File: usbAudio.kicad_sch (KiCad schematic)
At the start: 4 parts, among them J1 12V in, J2 USB_C_Receptacle_USB2.0_14P, J3 AudioJack3, U1 PCM2705CDBR

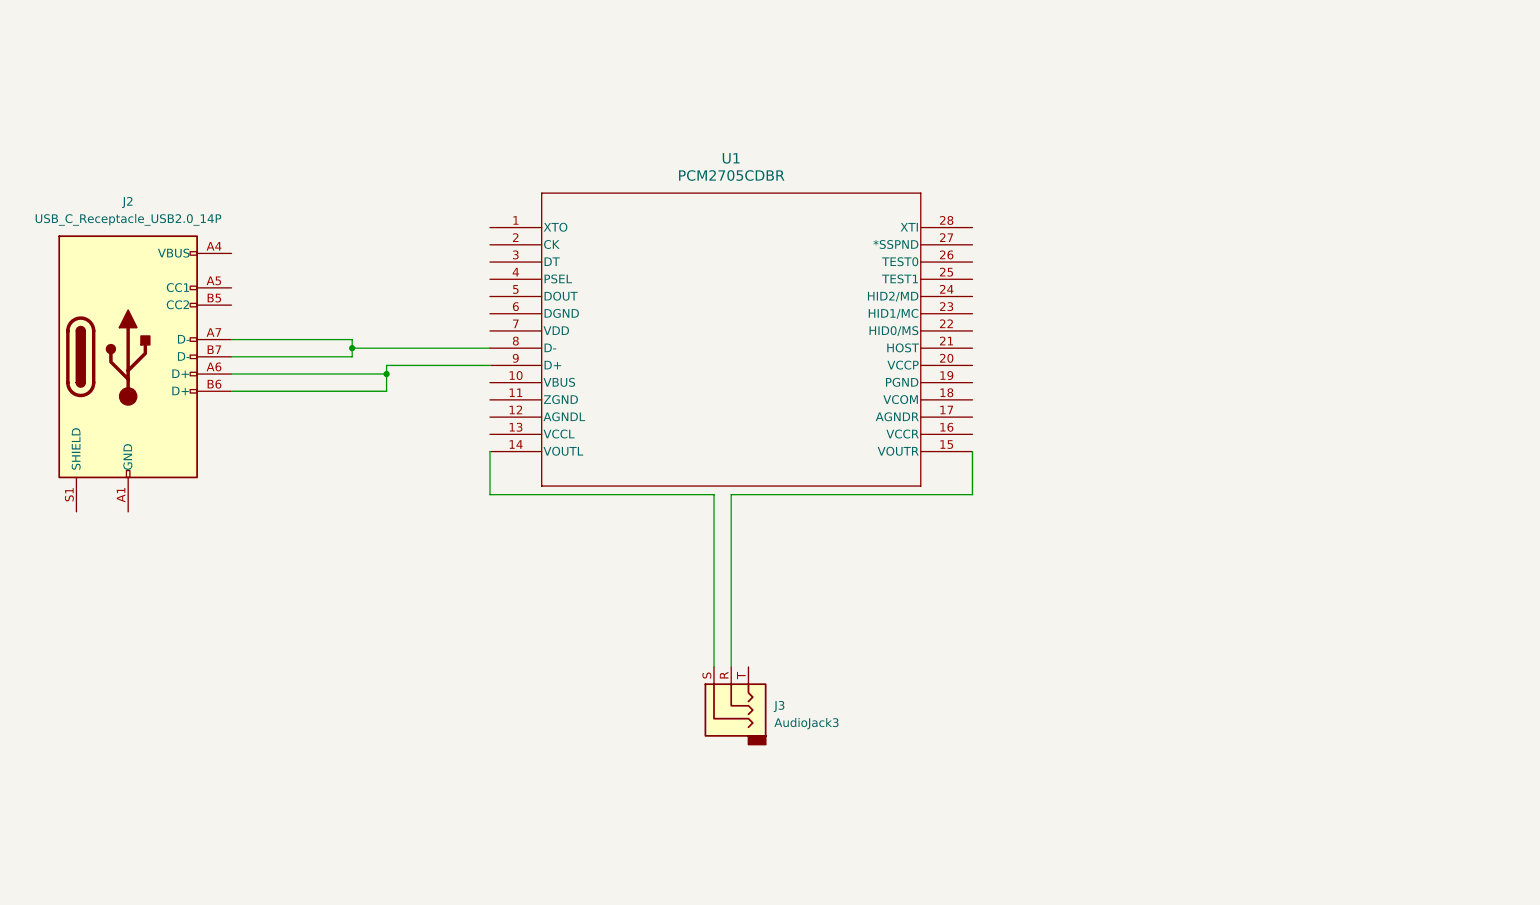
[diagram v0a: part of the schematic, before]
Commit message: Work on setting up audio IC
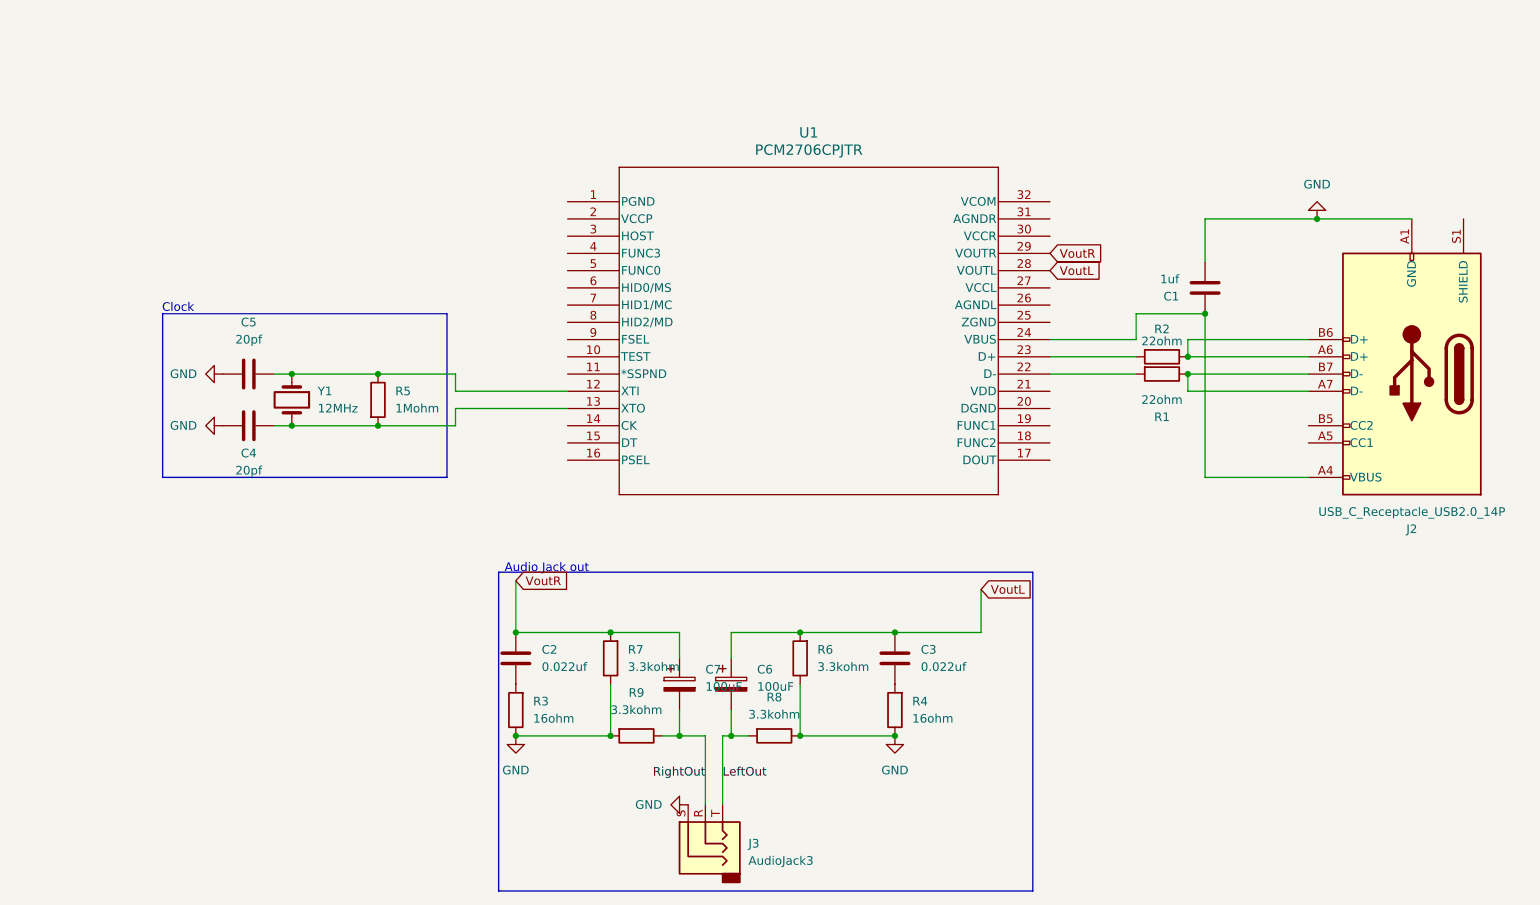
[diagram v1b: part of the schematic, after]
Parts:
- removed U1: PCM2705CDBR, DB28, symbol PCM2705C:PCM2705CDBR
- added C1: 1uf, symbol Device:C
- added C2, C3: 0.022uf, symbol Device:C
- added C4, C5: 20pf, symbol Device:C
- added C6, C7: 100uF, symbol Device:C_Polarized
- added R1, R2: 22ohm, symbol Device:R
- added R3, R4: 16ohm, symbol Device:R
- added R5: 1Mohm, symbol Device:R
- added R6, R7, R8, R9: 3.3kohm, symbol Device:R
- added U1: PCM2706CPJTR, PJT32, symbol PCM2706C:PCM2706CPJTR
- added Y1: 12MHz, symbol Device:Crystal
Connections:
- net RightOut: now reaches J3.R
- net RightOut: now also C7.2, R9.1
- net GND: now reaches J3.S
- net GND: now also J2.A1 (GND), J2.A12 (GND), J2.B1 (GND), J2.B12 (GND), C1.1, C4.2, C5.2, R3.1, R4.1, R6.1, R7.1, R8.1, R9.2
- net LeftOut: now reaches J3.T
- net LeftOut: now also C6.2, R8.2
- net at J2.A4 (VBUS), J2.A9 (VBUS), J2.B4 (VBUS)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: now also C1.2, U1.24 (VBUS)
- net at J2.A6 (D+), J2.B6 (D+): now also R2.1
- net at J2.A7 (D-), J2.B7 (D-): now also R1.1
- new net: C5.1, R5.1, U1.12 (XTI), Y1.1
- new net: C4.1, R5.2, U1.13 (XTO), Y1.2
- new net: R1.2, U1.22 (D-)
- new net: R2.2, U1.23 (D+)
- new net: C2.1, R3.2
- new net: C3.1, R4.2
- new net VoutL: C3.2, C6.1, R6.2, U1.28 (VOUTL)
- new net VoutR: C2.2, C7.1, R7.2, U1.29 (VOUTR)
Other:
- note added: "Audio Jack out"
- note added: "Clock"
- moved on the sheet: J2, J3

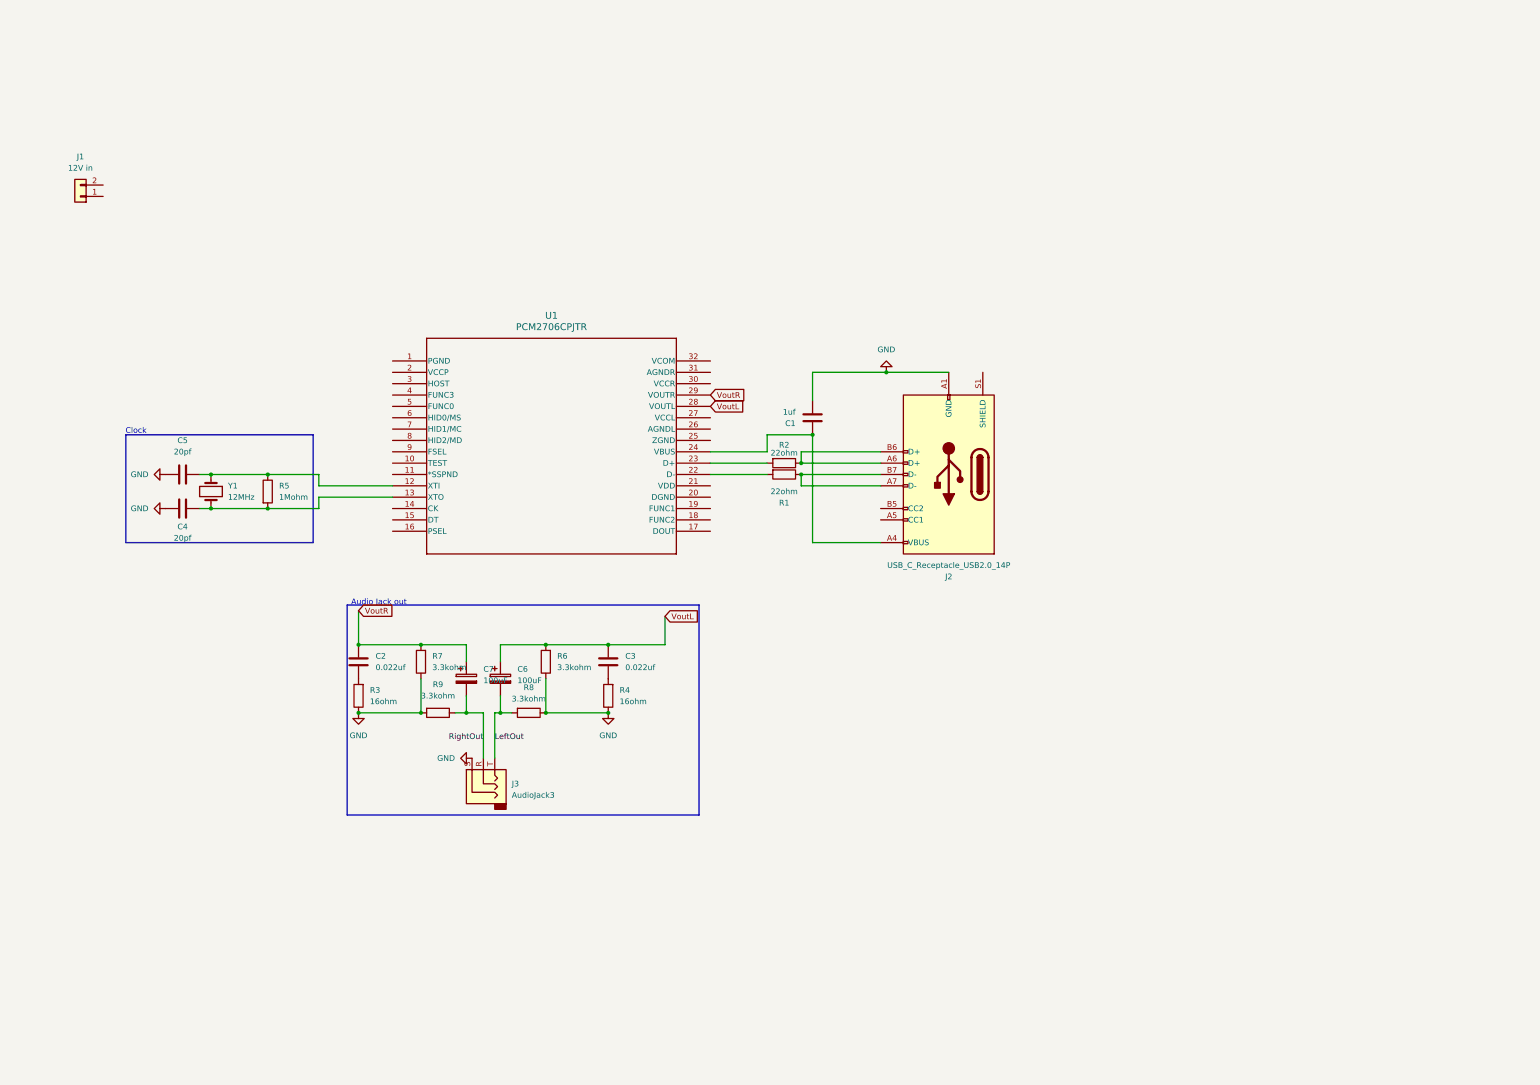
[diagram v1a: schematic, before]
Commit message: Finish audio IC
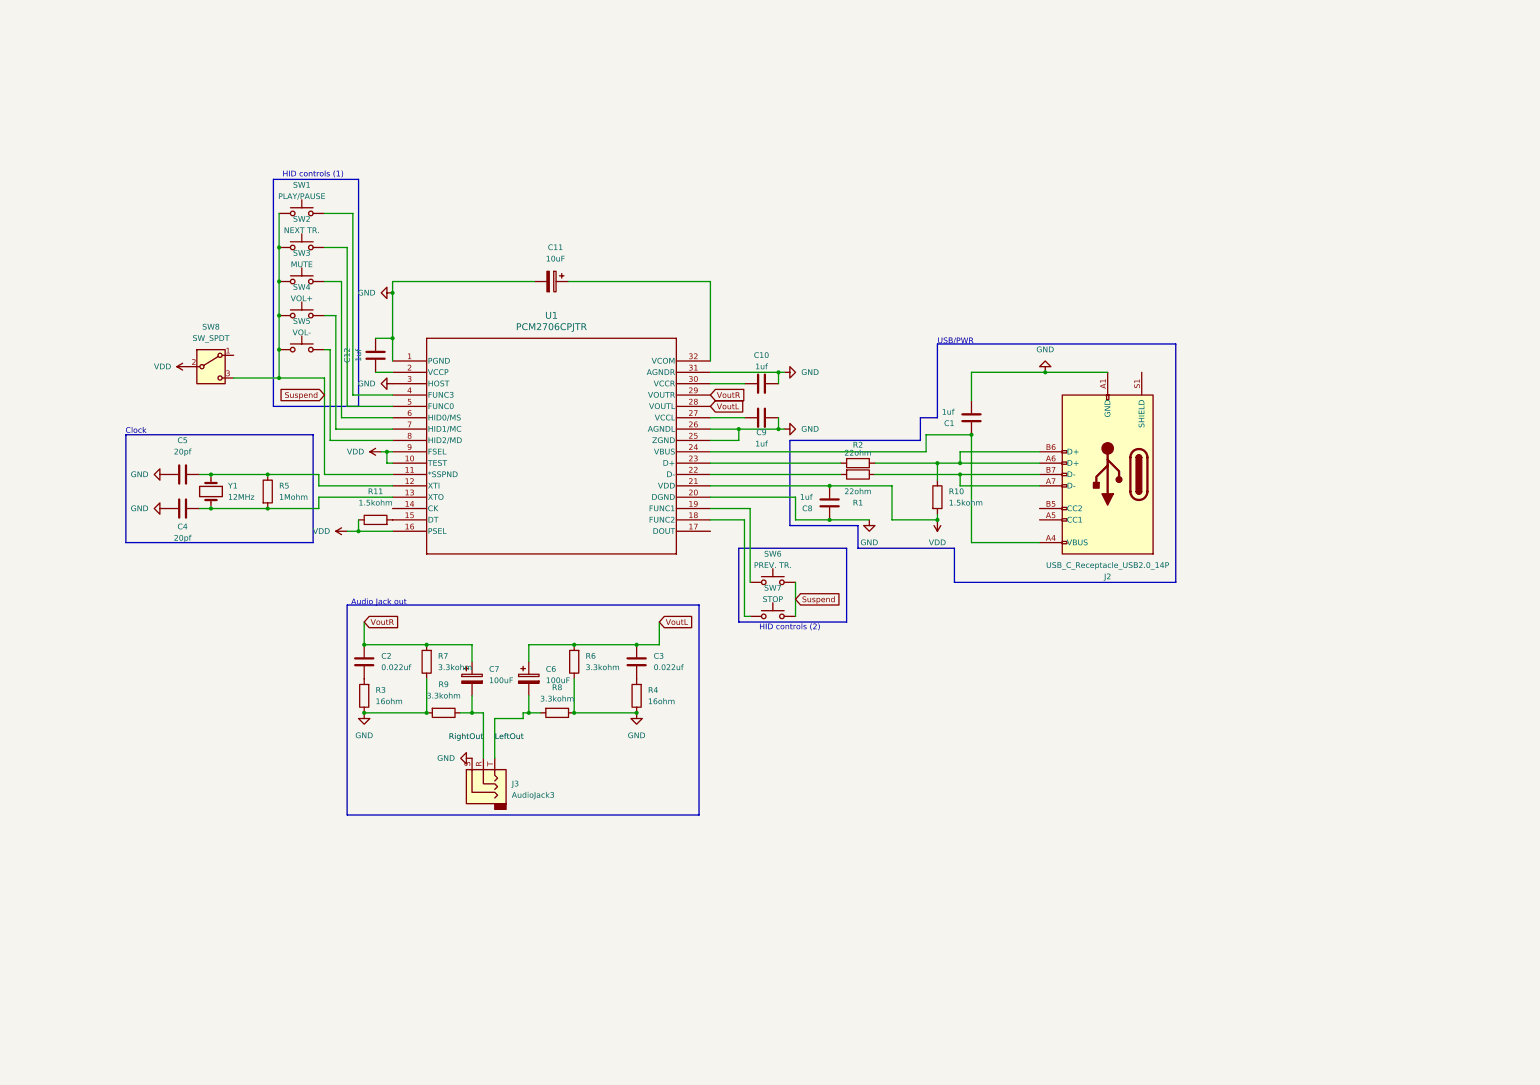
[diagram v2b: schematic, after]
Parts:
- removed J1: 12V in, symbol Connector_Generic:Conn_01x02
- added C10, C12, C8, C9: 1uf, symbol Device:C
- added C11: 10uF, symbol Device:C_Polarized
- added R10, R11: 1.5kohm, symbol Device:R
- added SW1: PLAY/PAUSE, symbol Switch:SW_Push
- added SW2: NEXT TR., symbol Switch:SW_Push
- added SW3: MUTE, symbol Switch:SW_Push
- added SW4: VOL+, symbol Switch:SW_Push
- added SW5: VOL-, symbol Switch:SW_Push
- added SW6: PREV. TR., symbol Switch:SW_Push
- added SW7: STOP, symbol Switch:SW_Push
- added SW8: SW_SPDT, symbol Switch:SW_SPDT
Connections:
- net GND: now also U1.1 (PGND), U1.20 (DGND), U1.25 (ZGND), U1.26 (AGNDL), U1.3 (HOST), U1.31 (AGNDR), C10.2, C11.2, C12.2, C8.2, C9.2
- net VDD: now reaches U1.10 (TEST)
- net VDD: now also U1.16 (PSEL), U1.21 (VDD), U1.9 (FSEL), C8.1, R10.2, R11.1, SW8.2 (B)
- net Suspend: now reaches U1.11 (*SSPND)
- net Suspend: now also SW1.1, SW2.1, SW3.1, SW4.1, SW5.1, SW6.2, SW7.2, SW8.3 (C)
- net at U1.15 (DT): now also R11.2
- net at U1.18 (FUNC2): now also SW7.1
- net at U1.19 (FUNC1): now also SW6.1
- net at U1.2 (VCCP): now also C12.1
- net at U1.27 (VCCL): now also C9.1
- net at U1.30 (VCCR): now also C10.1
- net at U1.32 (VCOM): now also C11.1
- net at U1.4 (FUNC3): now also SW1.2
- net at U1.5 (FUNC0): now also SW2.2
- net at U1.6 (HID0/MS): now also SW3.2
- net at U1.7 (HID1/MC): now also SW4.2
- net at U1.8 (HID2/MD): now also SW5.2
- net at J2.A6 (D+), J2.B6 (D+), R2.1: now also R10.1
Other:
- note added: "HID controls (1)"
- note added: "HID controls (2)"
- note added: "USB/PWR"
- moved on the sheet: C1, C2, C3, C6, C7, J2, R1, R2, R3, R4, R6, R7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

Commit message: Start work on power side
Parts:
- added C13: 0.1uf, symbol Device:C
- added C14: 150uf, symbol Device:C
- added C15, C16, C17: 47uf, symbol Device:C
- added R12: 100Kohm (1%), symbol Device:R
- added U2: TPS25810RVCR, RVC0020A, symbol TPS25810:TPS25810RVCR
- C1: value 1uf -> 10uf
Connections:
- net GND: now also C13.2, C15.2, C16.2, C17.2, U2.12 (GND), U2.21 (PAD)
- net cc1: now reaches J2.A5 (CC1)
- net cc1: now also U2.11 (CC1)
- net cc2: now reaches J2.B5 (CC2)
- net cc2: now also U2.13 (CC2)
- new net: R12.1, U2.10 (REF)
- new net: R12.2, U2.9 (REF_RTN)
- new net: C14.2, U2.14 (OUT), U2.15 (OUT)
- new net +5V: C13.1, C14.1, C15.1, C16.1, C17.1, U2.2 (IN1), U2.3 (IN1), U2.4 (IN2), U2.5 (AUX), U2.6 (EN), U2.7 (CHG), U2.8 (CHG_HI)
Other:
- note added: "USB faster charging"
- moved on the sheet: C1, C10, C11, C12, C2, C3, C4, C5, C6, C7, C8, C9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

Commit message: Finish schem!
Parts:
- removed C12: 1uf, symbol Device:C
- added C18: 100nF, symbol Device:C
- added C19: 22uF, symbol Device:C
- added C20: 10uF, symbol Device:C
- added C21, C22: 1uf, symbol Device:C
- added C23: 10uF, symbol Device:C_Polarized
- added J1: Conn_01x02, symbol Connector_Generic:Conn_01x02
- added L1: 4.7uH, symbol Device:L
- added U3: AP63205WU-7, AP63205:SOIC_05WU-7_DIO, symbol AP63205:AP63205WU-7
- added U4: MIC5504-3.3YM5-TR, SOT-23-5_MC_MCH, symbol MIC5504-3.3YM5:MIC5504-3.3YM5-TR
- C8: value 1uf -> 0.1uf
- R10: value 1.5kohm -> 3.3kohm
- U1: footprint PJT32 -> (none)
- U2: footprint RVC0020A -> TPS25810:RVC0020A
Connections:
- net +5V: now also C19.2, C22.1, L1.2, U3.1 (FB), U4.1 (VIN), U4.3 (EN); no longer U2.8 (CHG_HI)
- net GND: now also R10.1, U1.16 (PSEL), U2.8 (CHG_HI), C19.1, C20.1, C21.1, C22.2, C23.2, J1.1 (Pin_1), U3.4 (GND), U4.2 (GND); no longer U1.3 (HOST)
- net +3.3V: now reaches U1.2 (VCCP)
- net +3.3V: now also C10.1, C8.1, C9.1, R11.1, SW8.2 (B), U1.10 (TEST), U1.21 (VDD), U1.24 (VBUS), U1.27 (VCCL), U1.30 (VCCR), U1.9 (FSEL), C21.2, C23.1, U4.5 (VOUT)
- net Vbus: now reaches C1.2, J2.A4 (VBUS), J2.A9 (VBUS), J2.B4 (VBUS), J2.B9 (VBUS)
- net Vbus: now also C14.2, R10.2, U1.3 (HOST), U2.14 (OUT), U2.15 (OUT); no longer U1.24 (VBUS)
- net at J2.A6 (D+), J2.B6 (D+), R2.1: no longer R10.1
- removed net VDD: C8.1, R10.2, R11.1, SW8.2 (B), U1.10 (TEST), U1.16 (PSEL), U1.21 (VDD), U1.9 (FSEL)
- new net: C18.2, L1.1, U3.5 (SW)
- new net: C18.1, U3.6 (BST)
- new net +12V: C20.2, J1.2 (Pin_2), U3.2 (EN), U3.3 (VIN)
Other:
- note added: "12 - 5V conv"
- note added: "3.3V source"
- moved on the sheet: C1, C10, C2, C3, C6, C7, C9, J2, J3, R3, R4, R6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
